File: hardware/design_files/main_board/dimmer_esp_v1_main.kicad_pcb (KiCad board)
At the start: 2 copper layers, 44 x 49.5 mm, 46 parts, among them IC1 PEC11S-929K-S0015, J1 SM05B-SRSS-TB_LF__SN_, J4 Conn_01x02, J5 Conn_01x02, J6 Conn_01x02, J7 Conn_01x04, J8 Screw_Terminal_01x03, K2 FINDER-34.51, SW1 Commission, SW2 Reset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

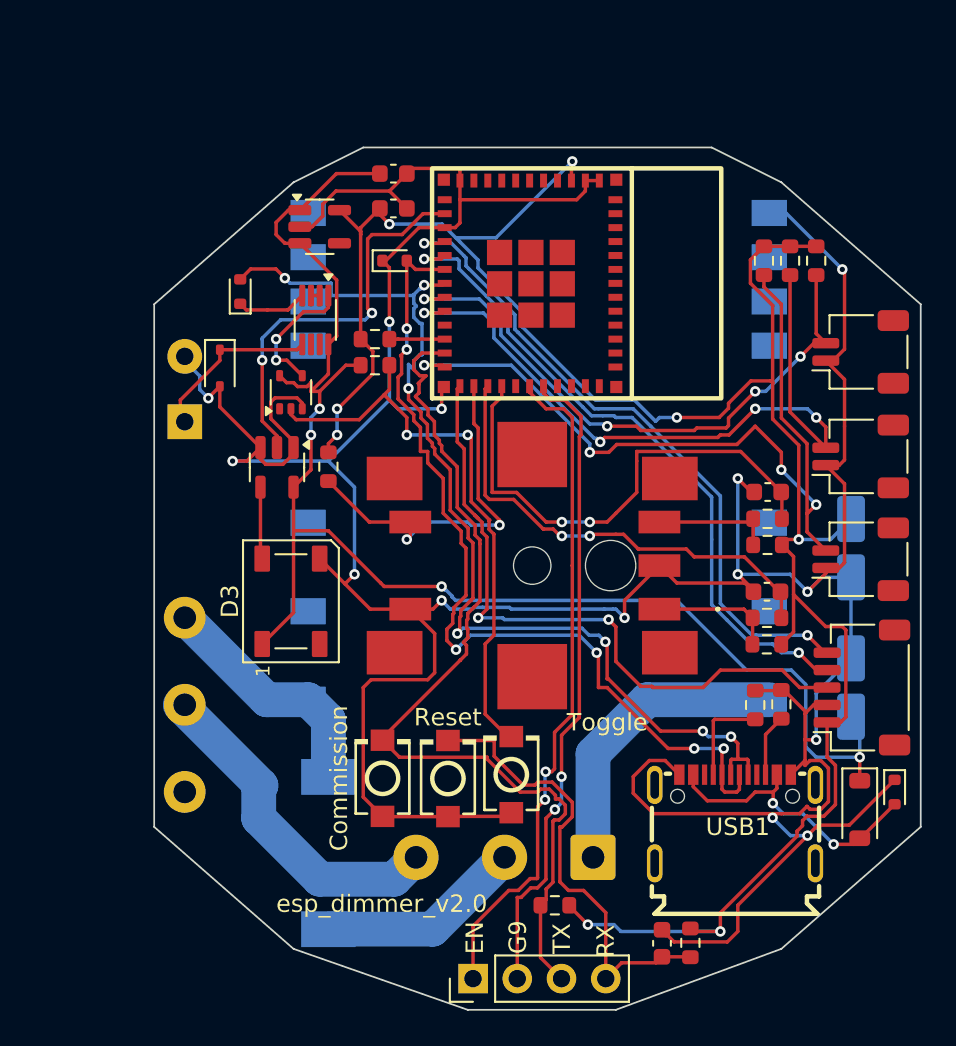
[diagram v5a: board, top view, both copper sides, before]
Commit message: Add circuit for external encoder
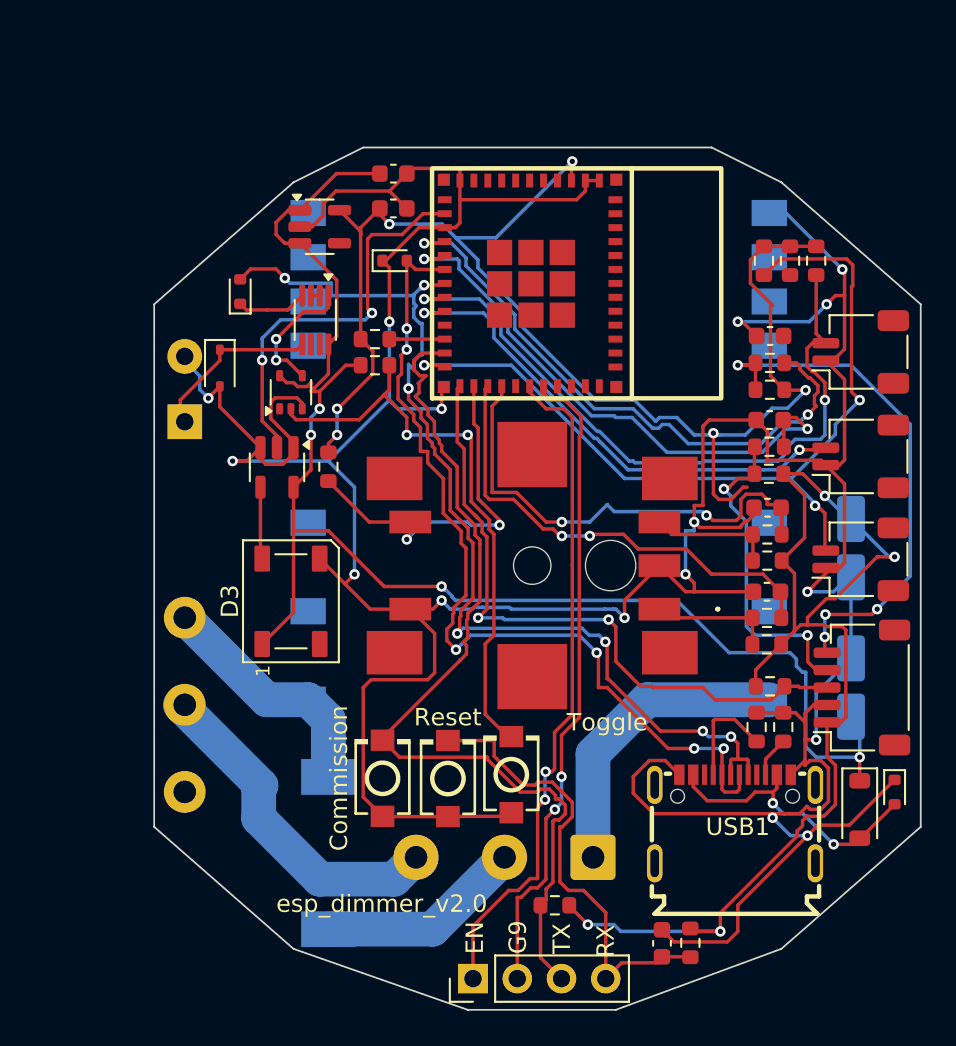
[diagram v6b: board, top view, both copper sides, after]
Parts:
- added C8: 0.01u, Capacitor_SMD:C_0603_1608Metric, F.Cu at (180.9, 47.8)
- added C9: 0.01u, Capacitor_SMD:C_0603_1608Metric, F.Cu at (180.8, 52.6)
- added R15: 10k, Resistor_SMD:R_0603_1608Metric, F.Cu at (180.8, 50.9)
- added R16: 10k, Resistor_SMD:R_0603_1608Metric, F.Cu at (180.8, 55.7)
- added R17: 10k, Resistor_SMD:R_0603_1608Metric, F.Cu at (180.8, 49.4)
- added R18: 10k, Resistor_SMD:R_0603_1608Metric, F.Cu at (180.8, 54.2)
- added R19: 10k, Resistor_SMD:R_0603_1608Metric, F.Cu at (180.9, 67.9)
- moved R6 1.31 mm to (181.6, 70.3)
- moved R5 1.27 mm to (180.1, 70.3)
- moved R1 0.90 mm to (180.7, 60.7)
- moved R4 0.90 mm to (180.7, 59.2)
- moved C2 0.90 mm to (180.7, 57.7)
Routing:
- net Net-(J1-Pad5): track 0.00 -> 30.9 mm, vias 0 -> 4
- net GND: track 242.7 -> 262.6 mm, vias 14 -> 16
- net +3.3V: track 125.8 -> 145.0 mm, vias 8 -> 10
- net Net-(J1-Pad4): track 0.00 -> 18.7 mm, vias 0 -> 2
- net /D15: track 40.8 -> 28.9 mm, vias 4 -> 2
- net /D07: track 38.5 -> 32.4 mm
- net /D14: track 34.5 -> 40.1 mm, vias 4 -> 2
- net /D06: track 38.3 -> 34.0 mm
- net /D18: track 47.0 -> 49.6 mm, vias 4 -> 3
- net Net-(USB1-CC2): track 3.59 -> 2.33 mm
- net /D22: track 29.1 -> 27.9 mm
- net +5V: track 84.5 -> 85.2 mm
- net Net-(USB1-CC1): track 5.54 -> 6.14 mm

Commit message: Add correct relay
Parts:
- removed K2: FINDER-34.51, Relay_THT:Relay_SPDT_Finder_34.51_Vertical
- added K1: FTR-LYCA005Y, relay_mouser:FTRLYCA024Y, B.Cu at (147.6, 48.5)
- moved D6 0.73 mm to (150.0, 49.7)
- moved C9 0.08 mm to (180.8, 52.7)
- moved C8 0.07 mm to (180.8, 47.9)
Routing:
- net +3.3V: track 145.0 -> 147.3 mm
- net Net-(D6-K): track 9.94 -> 9.24 mm

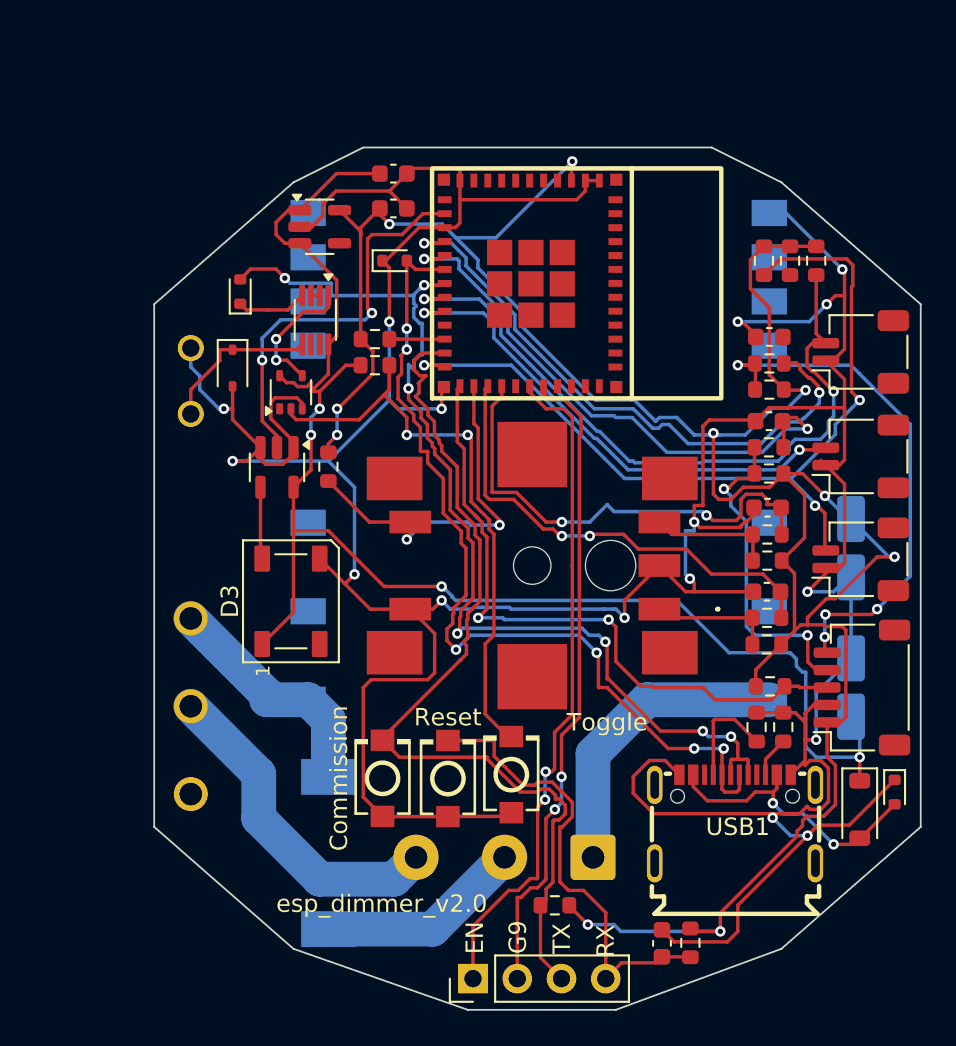
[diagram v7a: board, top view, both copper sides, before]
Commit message: Add correct USB, fix button layout
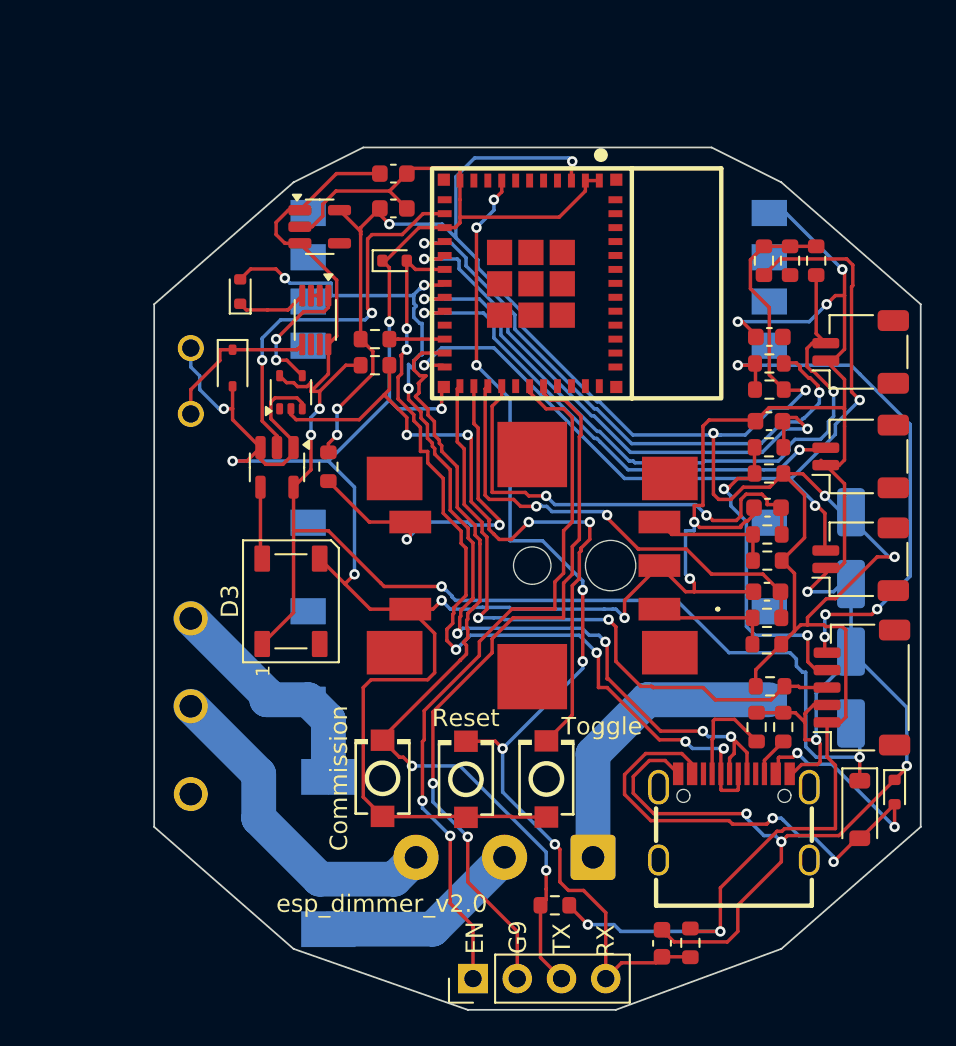
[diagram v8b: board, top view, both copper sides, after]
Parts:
- removed USB1: USB-C: GT-USB-7016, usb_jlc:USB-C-SMD_GT-USB-7016B
- added USB2: USB-TYPE-C-018, usb_jlc:USB-C_SMD-TYPE-C-31-M-12, F.Cu at (178.8, 75.4)
- C3, C4: footprint Capacitor_SMD:C_Elec_4x5.4 -> Capacitor_SMD:C_Elec_5x5.4
- U4: value SN74LV1T125DBV -> SN74LV1T125DBVR
- U6: value SN74LVC1G74 -> SN74LVC1G74DCUR
- moved SW3 2.03 mm to (168.0, 73.2)
- moved SW2 1.03 mm to (163.4, 73.3)
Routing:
- net /EN: track 26.6 -> 62.4 mm, vias 0 -> 7
- net Net-(D1-A2): track 15.9 -> 35.5 mm, vias 2 -> 4
- net Net-(R13-Pad2): track 33.6 -> 40.5 mm, vias 2 -> 4
- net /UART_TXD: track 37.3 -> 42.6 mm
- net /D09: track 52.1 -> 48.5 mm, vias 0 -> 2
- net +3.3V: track 147.3 -> 150.6 mm
- net /UART_RXD: track 38.8 -> 41.8 mm
- net GND: track 263.0 -> 264.6 mm, vias 16 -> 17
- net /D22: track 27.9 -> 27.1 mm
- net /D18: track 49.6 -> 50.5 mm
- net /D13: track 60.2 -> 60.8 mm
